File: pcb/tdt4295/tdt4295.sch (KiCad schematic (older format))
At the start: 44 parts, among them J101 ARM 20 Pin Debug Header, J102 DM1AA-SF-PEJ(21), J103 MCU USART1 Header, J104 MCU GPIO Header, U101 EFM32GG12B810F1024GQ64, U102 COM-09032 Joystick, U103 COM-09032 Joystick, Y101 48MHz

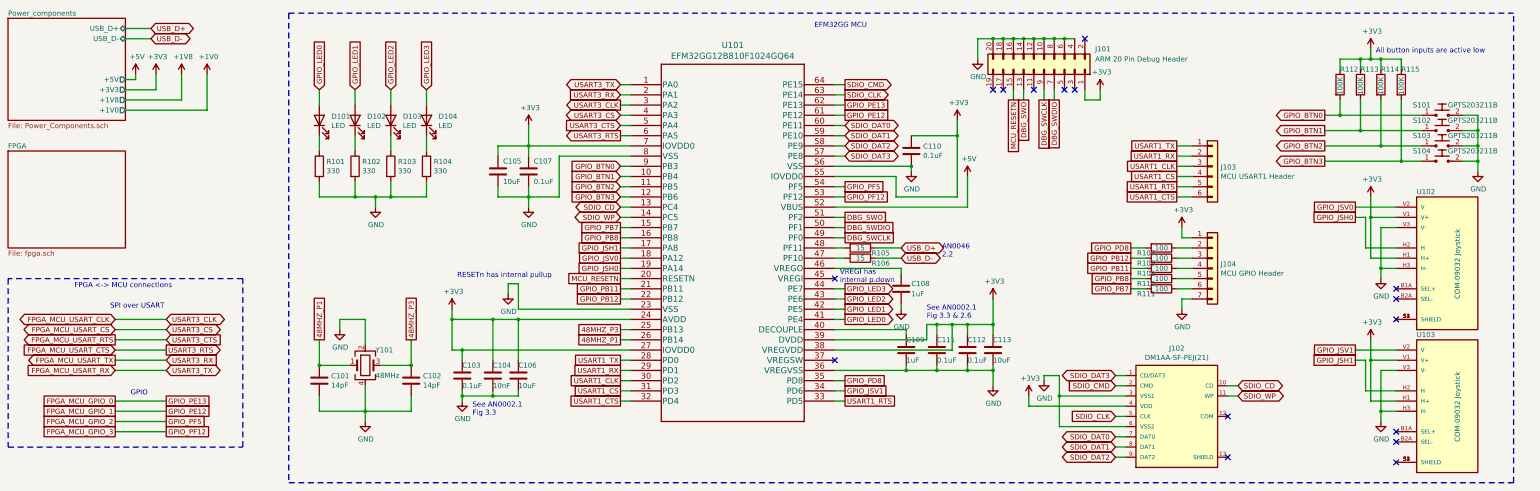
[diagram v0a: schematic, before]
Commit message: MCU fixes from review comments
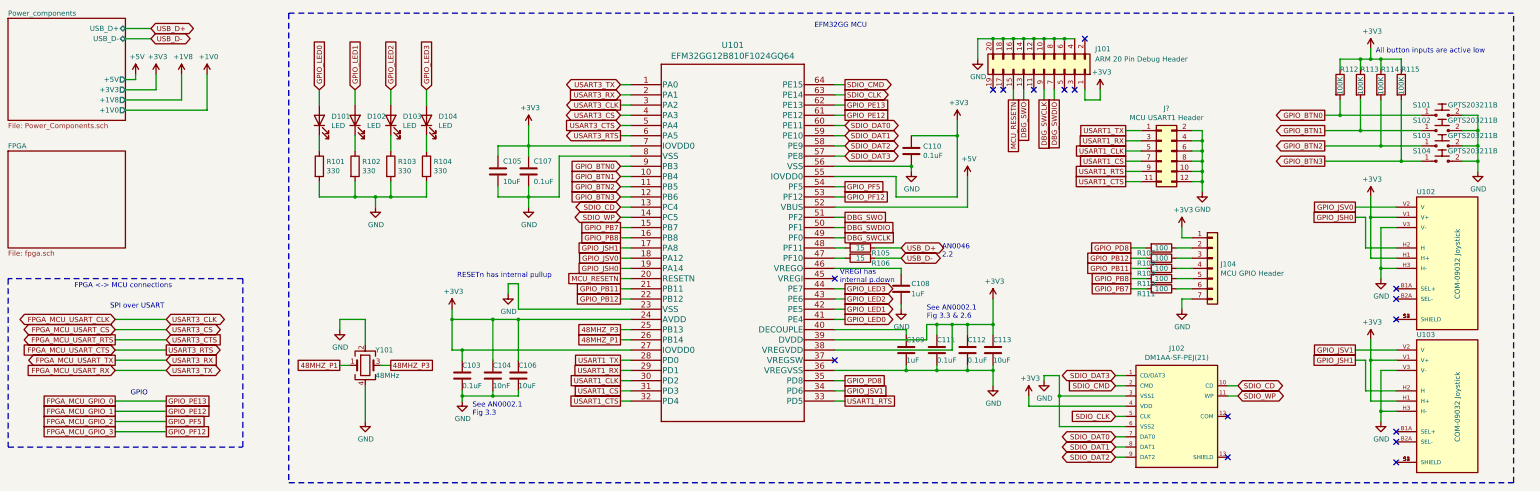
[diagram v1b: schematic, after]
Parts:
- removed C101, C102: 14pF, Capacitor_SMD:C_1210_3225Metric_Pad1.33x2.70mm_HandSolder, symbol Device:C
- removed J103: MCU USART1 Header, Connector_PinSocket_2.54mm:PinSocket_1x06_P2.54mm_Vertical, symbol Connector_Generic:Conn_01x06
- added J?: MCU USART1 Header, symbol Connector_Generic:Conn_02x06_Odd_Even
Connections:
- net GND: now also J?.10 (Pin_10), J?.12 (Pin_12), J?.2 (Pin_2), J?.4 (Pin_4), J?.6 (Pin_6), J?.8 (Pin_8)
- net USART1_CLK: now also J?.5 (Pin_5)
- net USART1_CS: now also J?.7 (Pin_7)
- net USART1_CTS: now also J?.11 (Pin_11)
- net USART1_RTS: now also J?.9 (Pin_9)
- net USART1_RX: now also J?.3 (Pin_3)
- net USART1_TX: now also J?.1 (Pin_1)
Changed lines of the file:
@@
 	4000 3900 4000 4000
 Wire Wire Line
-	4400 4350 4700 4350
-Wire Wire Line
-	4250 4900 4250 4800
-Wire Wire Line
-	4250 4550 4250 4800
-Connection ~ 4250 4800
-Wire Wire Line
-	3800 4800 3800 4650
-Wire Wire Line
-	4250 4800 3800 4800
-Wire Wire Line
-	4700 4800 4700 4650
-Wire Wire Line
-	4250 4800 4700 4800
+	4400 4350 4500 4350
 Wire Wire Line
 	4250 4150 4250 3900
@@
 $EndComp
 $Comp
-L Device:C C102
-U 1 1 6146ECCE
-P 4700 4500
-F 0 "C102" H 4815 4546 50  0000 L CNN
-F 1 "14pF" H 4815 4455 50  0000 L CNN
-F 2 "Capacitor_SMD:C_1210_3225Metric_Pad1.33x2.70mm_HandSolder" H 4738 4350 50  0001 C CNN
-F 3 "https://api.kemet.com/component-edge/download/specsheet/C1210C107M9PACTU.pdf" H 4700 4500 50  0001 C CNN
-F 4 "" H 4700 4500 50  0001 C CNN "Category"
-F 5 "https://no.farnell.com/kemet/c1210c107m9pactu/cap-100-f-6-3v-20-x5r-1210/dp/1108328?st=c1210c107m9pactu" H 4700 4500 50  0001 C CNN "DK_Detail_Page"
-F 6 "C1210C107M9PACTU" H 4700 4500 50  0001 C CNN "Component name"
-	1    4700 4500
-	1    0    0    -1
-$EndComp
-$Comp
-L Device:C C101
-U 1 1 6146E505
-P 3800 4500
-F 0 "C101" H 3915 4546 50  0000 L CNN
-F 1 "14pF" H 3915 4455 50  0000 L CNN
-F 2 "Capacitor_SMD:C_1210_3225Metric_Pad1.33x2.70mm_HandSolder" H 3838 4350 50  0001 C CNN
-F 3 "https://api.kemet.com/component-edge/download/specsheet/C1210C107M9PACTU.pdf" H 3800 4500 50  0001 C CNN
-F 4 "" H 3800 4500 50  0001 C CNN "Category"
-F 5 "https://no.farnell.com/kemet/c1210c107m9pactu/cap-100-f-6-3v-20-x5r-1210/dp/1108328?st=c1210c107m9pactu" H 3800 4500 50  0001 C CNN "DK_Detail_Page"
-F 6 "C1210C107M9PACTU" H 3800 4500 50  0001 C CNN "Component name"
-	1    3800 4500
-	1    0    0    -1
-$EndComp
-$Comp
 L power:GND #PWR0106
 U 1 1 6146D608
@@
 	1    0    0    -1
 $EndComp
-Text GLabel 4700 4100 1    50   UnSpc ~ 0
+Text GLabel 4500 4350 2    50   UnSpc ~ 0
 48MHZ_P3
-Text GLabel 3800 4100 1    50   UnSpc ~ 0
+Text GLabel 4000 4350 0    50   UnSpc ~ 0
 48MHZ_P1
 Wire Wire Line
-	3800 4100 3800 4350
-Wire Wire Line
-	4700 4100 4700 4350
-Connection ~ 4700 4350
-Wire Wire Line
-	3800 4350 4100 4350
-Connection ~ 3800 4350
+	4000 4350 4100 4350
 Text GLabel 6750 4000 0    50   UnSpc ~ 0
 48MHZ_P3
@@
 Text GLabel 11750 3200 0    50   UnSpc ~ 0
 GPIO_PD8
-$Comp
-L Connector_Generic:Conn_01x06 J103
-U 1 1 61BFE8BD
-P 12550 2400
-F 0 "J103" H 12630 2392 50  0000 L CNN
-F 1 "MCU USART1 Header" H 12630 2301 50  0000 L CNN
-F 2 "Connector_PinSocket_2.54mm:PinSocket_1x06_P2.54mm_Vertical" H 12550 2400 50  0001 C CNN
-F 3 "~" H 12550 2400 50  0001 C CNN
-	1    12550 2400
-	1    0    0    -1
-$EndComp
-Text GLabel 12200 2200 0    50   UnSpc ~ 0
+Text GLabel 11700 2050 0    50   UnSpc ~ 0
 USART1_TX
-Text GLabel 12200 2300 0    50   UnSpc ~ 0
+Text GLabel 11700 2150 0    50   UnSpc ~ 0
 USART1_RX
-Text GLabel 12200 2400 0    50   UnSpc ~ 0
+Text GLabel 11700 2250 0    50   UnSpc ~ 0
 USART1_CLK
-Text GLabel 12200 2500 0    50   UnSpc ~ 0
+Text GLabel 11700 2350 0    50   UnSpc ~ 0
 USART1_CS
-Text GLabel 12200 2600 0    50   UnSpc ~ 0
+Text GLabel 11700 2450 0    50   UnSpc ~ 0
 USART1_RTS
-Text GLabel 12200 2700 0    50   UnSpc ~ 0
+Text GLabel 11700 2550 0    50   UnSpc ~ 0
 USART1_CTS
 Wire Wire Line
-	12200 2200 12350 2200
-Wire Wire Line
-	12350 2300 12200 2300
-Wire Wire Line
-	12200 2400 12350 2400
-Wire Wire Line
-	12350 2500 12200 2500
-Wire Wire Line
-	12200 2600 12350 2600
-Wire Wire Line
-	12350 2700 12200 2700
+	11700 2050 11850 2050
+Wire Wire Line
+	11850 2150 11700 2150
+Wire Wire Line
+	11700 2250 11850 2250
+Wire Wire Line
+	11850 2350 11700 2350
+Wire Wire Line
+	11700 2450 11850 2450
+Wire Wire Line
+	11850 2550 11700 2550
 $Comp
 L power:GND #PWR0130
@@
 Text GLabel 11600 4550 0    50   Input ~ 0
 SDIO_CMD
+$Comp
+L Connector_Generic:Conn_02x06_Odd_Even J?
+U 1 1 61568E09
+P 12050 2250
+F 0 "J?" H 12100 2667 50  0000 C CNN
+F 1 "MCU USART1 Header" H 12100 2576 50  0000 C CNN
+F 2 "" H 12050 2250 50  0001 C CNN
+F 3 "~" H 12050 2250 50  0001 C CNN
+	1    12050 2250
+	1    0    0    -1
+$EndComp
+$Comp
+L power:GND #PWR?
+U 1 1 61580AEB
+P 12450 2650
+F 0 "#PWR?" H 12450 2400 50  0001 C CNN
+F 1 "GND" H 12455 2477 50  0000 C CNN
+F 2 "" H 12450 2650 50  0001 C CNN
+F 3 "" H 12450 2650 50  0001 C CNN
+	1    12450 2650
+	1    0    0    -1
+$EndComp
+Wire Wire Line
+	12450 2650 12450 2550
+Wire Wire Line
+	12450 2550 12350 2550
+Wire Wire Line
+	12450 2550 12450 2450
+Wire Wire Line
+	12450 2450 12350 2450
+Connection ~ 12450 2550
+Wire Wire Line
+	12350 2350 12450 2350
+Wire Wire Line
+	12450 2350 12450 2450
+Connection ~ 12450 2450
+Wire Wire Line
+	12350 2250 12450 2250
+Wire Wire Line
+	12450 2250 12450 2350
+Connection ~ 12450 2350
+Wire Wire Line
+	12350 2150 12450 2150
+Wire Wire Line
+	12450 2150 12450 2250
+Connection ~ 12450 2250
+Wire Wire Line
+	12350 2050 12450 2050
+Wire Wire Line
+	12450 2050 12450 2150
+Connection ~ 12450 2150
+Wire Wire Line
+	4250 4550 4250 4900
 $EndSCHEMATC

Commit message: add footprints, rename components
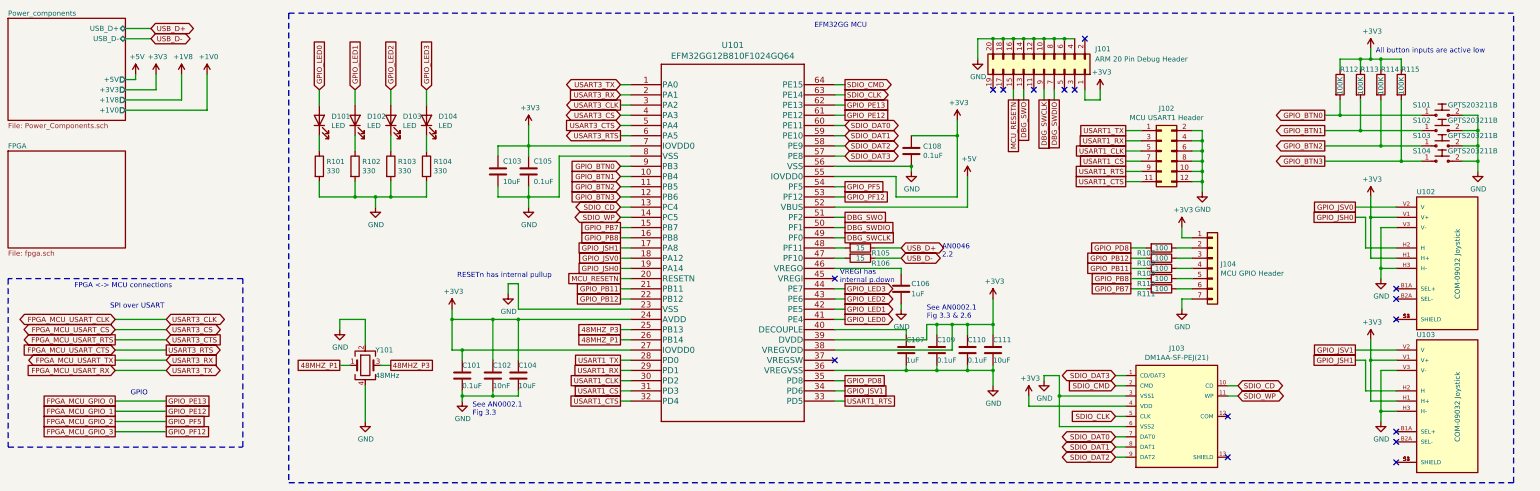
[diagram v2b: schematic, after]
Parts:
- J102: renamed from J?; footprint (none) -> Connector_PinHeader_2.54mm:PinHeader_2x06_P2.54mm_Vertical
- renumbered C103 to C101, C104 to C102, C105 to C103, C106 to C104, C107 to C105, C108 to C106, C109 to C107, C110 to C108, C111 to C109, C112 to C110, C113 to C111, J102 to J103
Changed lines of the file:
@@
 	10050 1950 10050 2100
 $Comp
-L Device:C C110
+L Device:C C108
 U 1 1 614780F2
 P 9600 2250
-F 0 "C110" H 9715 2296 50  0000 L CNN
+F 0 "C108" H 9715 2296 50  0000 L CNN
 F 1 "0.1uF" H 9715 2205 50  0000 L CNN
 F 2 "Capacitor_SMD:C_0603_1608Metric_Pad1.08x0.95mm_HandSolder" H 9638 2100 50  0001 C CNN
@@
 $EndComp
 $Comp
-L Device:C C103
+L Device:C C101
 U 1 1 614CD408
 P 5200 4450
-F 0 "C103" H 5200 4550 50  0000 L CNN
+F 0 "C101" H 5200 4550 50  0000 L CNN
 F 1 "0.1uF" H 5200 4350 50  0000 L CNN
 F 2 "Capacitor_SMD:C_0603_1608Metric_Pad1.08x0.95mm_HandSolder" H 5238 4300 50  0001 C CNN
@@
 Connection ~ 5200 4200
 $Comp
-L Device:C C107
+L Device:C C105
 U 1 1 614EE588
 P 5850 2450
-F 0 "C107" H 5900 2550 50  0000 L CNN
+F 0 "C105" H 5900 2550 50  0000 L CNN
 F 1 "0.1uF" H 5900 2350 50  0000 L CNN
 F 2 "Capacitor_SMD:C_0603_1608Metric_Pad1.08x0.95mm_HandSolder" H 5888 2300 50  0001 C CNN
@@
 Connection ~ 5850 2200
 $Comp
-L Device:C C105
+L Device:C C103
 U 1 1 6153B508
 P 5550 2450
-F 0 "C105" H 5600 2550 50  0000 L CNN
+F 0 "C103" H 5600 2550 50  0000 L CNN
 F 1 "10uF" H 5600 2350 50  0000 L CNN
 F 2 "Capacitor_SMD:C_0603_1608Metric_Pad1.08x0.95mm_HandSolder" H 5588 2300 50  0001 C CNN
@@
 	5850 2200 6850 2200
 $Comp
-L Device:C C109
+L Device:C C107
 U 1 1 6145F357
 P 9550 4200
-F 0 "C109" H 9550 4300 50  0000 L CNN
+F 0 "C107" H 9550 4300 50  0000 L CNN
 F 1 "1uF" H 9550 4100 50  0000 L CNN
 F 2 "Capacitor_SMD:C_0603_1608Metric_Pad1.08x0.95mm_HandSolder" H 9588 4050 50  0001 C CNN
@@
 $EndComp
 $Comp
-L Device:C C104
+L Device:C C102
 U 1 1 615F1A43
 P 5500 4450
-F 0 "C104" H 5500 4550 50  0000 L CNN
+F 0 "C102" H 5500 4550 50  0000 L CNN
 F 1 "10nF" H 5500 4350 50  0000 L CNN
 F 2 "Capacitor_SMD:C_0603_1608Metric_Pad1.08x0.95mm_HandSolder" H 5538 4300 50  0001 C CNN
@@
 $EndComp
 $Comp
-L Device:C C106
+L Device:C C104
 U 1 1 615F24C1
 P 5750 4450
-F 0 "C106" H 5750 4550 50  0000 L CNN
+F 0 "C104" H 5750 4550 50  0000 L CNN
 F 1 "10uF" H 5750 4350 50  0000 L CNN
 F 2 "Capacitor_SMD:C_0603_1608Metric_Pad1.08x0.95mm_HandSolder" H 5788 4300 50  0001 C CNN
@@
 $EndComp
 $Comp
-L Device:C C113
+L Device:C C111
 U 1 1 61654772
 P 10400 4200
-F 0 "C113" H 10400 4300 50  0000 L CNN
+F 0 "C111" H 10400 4300 50  0000 L CNN
 F 1 "10uF" H 10400 4100 50  0000 L CNN
 F 2 "Capacitor_SMD:C_0603_1608Metric_Pad1.08x0.95mm_HandSolder" H 10438 4050 50  0001 C CNN
@@
 $EndComp
 $Comp
-L Device:C C112
+L Device:C C110
 U 1 1 61654C00
 P 10150 4200
-F 0 "C112" H 10150 4300 50  0000 L CNN
+F 0 "C110" H 10150 4300 50  0000 L CNN
 F 1 "0.1uF" H 10150 4100 50  0000 L CNN
 F 2 "Capacitor_SMD:C_0603_1608Metric_Pad1.08x0.95mm_HandSolder" H 10188 4050 50  0001 C CNN
@@
 	10000 3950 10150 3950
 $Comp
-L Device:C C111
+L Device:C C109
 U 1 1 61724FBA
 P 9850 4200
-F 0 "C111" H 9850 4300 50  0000 L CNN
+F 0 "C109" H 9850 4300 50  0000 L CNN
 F 1 "0.1uF" H 9850 4100 50  0000 L CNN
 F 2 "Capacitor_SMD:C_0603_1608Metric_Pad1.08x0.95mm_HandSolder" H 9888 4050 50  0001 C CNN
@@
 AN0046\n2.2
 $Comp
-L Device:C C108
+L Device:C C106
 U 1 1 618F8B31
 P 9500 3600
-F 0 "C108" H 9600 3650 50  0000 L CNN
+F 0 "C106" H 9600 3650 50  0000 L CNN
 F 1 "1uF" H 9600 3550 50  0000 L CNN
 F 2 "Capacitor_SMD:C_0603_1608Metric_Pad1.08x0.95mm_HandSolder" H 9538 3450 50  0001 C CNN
@@
 	15150 1900 15000 1900
 $Comp
-L power:+3V3 #PWR0125
+L power:+3V3 #PWR0126
 U 1 1 614E0EAB
 P 14100 1250
-F 0 "#PWR0125" H 14100 1100 50  0001 C CNN
+F 0 "#PWR0126" H 14100 1100 50  0001 C CNN
 F 1 "+3V3" H 14115 1423 50  0000 C CNN
 F 2 "" H 14100 1250 50  0001 C CNN
@@
 	11850 2550 11700 2550
 $Comp
-L power:GND #PWR0130
+L power:GND #PWR0131
 U 1 1 615042CB
 P 15150 2450
-F 0 "#PWR0130" H 15150 2200 50  0001 C CNN
+F 0 "#PWR0131" H 15150 2200 50  0001 C CNN
 F 1 "GND" H 15155 2277 50  0000 C CNN
 F 2 "" H 15150 2450 50  0001 C CNN
@@
 NoConn ~ 14350 3900
 $Comp
-L power:+3V3 #PWR0126
+L power:+3V3 #PWR0127
 U 1 1 615D21D5
 P 14100 2700
-F 0 "#PWR0126" H 14100 2550 50  0001 C CNN
+F 0 "#PWR0127" H 14100 2550 50  0001 C CNN
 F 1 "+3V3" H 14115 2873 50  0000 C CNN
 F 2 "" H 14100 2700 50  0001 C CNN
@@
 NoConn ~ 14350 3700
 $Comp
-L power:GND #PWR0128
+L power:GND #PWR0129
 U 1 1 61621364
 P 14200 3500
-F 0 "#PWR0128" H 14200 3250 50  0001 C CNN
+F 0 "#PWR0129" H 14200 3250 50  0001 C CNN
 F 1 "GND" H 14205 3327 50  0000 C CNN
 F 2 "" H 14200 3500 50  0001 C CNN
@@
 NoConn ~ 14350 5300
 $Comp
-L power:+3V3 #PWR0127
+L power:+3V3 #PWR0128
 U 1 1 616BCC96
 P 14100 4100
-F 0 "#PWR0127" H 14100 3950 50  0001 C CNN
+F 0 "#PWR0128" H 14100 3950 50  0001 C CNN
 F 1 "+3V3" H 14115 4273 50  0000 C CNN
 F 2 "" H 14100 4100 50  0001 C CNN
@@
 NoConn ~ 14350 5100
 $Comp
-L power:GND #PWR0129
+L power:GND #PWR0130
 U 1 1 616BCCA3
 P 14200 4900
-F 0 "#PWR0129" H 14200 4650 50  0001 C CNN
+F 0 "#PWR0130" H 14200 4650 50  0001 C CNN
 F 1 "GND" H 14205 4727 50  0000 C CNN
 F 2 "" H 14200 4900 50  0001 C CNN
@@
 NoConn ~ 12700 4850
 $Comp
-L DM1AA-SF-PEJ_21_:DM1AA-SF-PEJ(21) J102
+L DM1AA-SF-PEJ_21_:DM1AA-SF-PEJ(21) J103
 U 1 1 61599B42
 P 12200 4850
-F 0 "J102" H 12200 5517 50  0000 C CNN
+F 0 "J103" H 12200 5517 50  0000 C CNN
 F 1 "DM1AA-SF-PEJ(21)" H 12200 5426 50  0000 C CNN
 F 2 "HRS_DM1AA-SF-PEJ(21)" H 12200 4850 50  0001 L BNN
@@
 SDIO_CMD
 $Comp
-L Connector_Generic:Conn_02x06_Odd_Even J?
+L Connector_Generic:Conn_02x06_Odd_Even J102
 U 1 1 61568E09
 P 12050 2250
-F 0 "J?" H 12100 2667 50  0000 C CNN
+F 0 "J102" H 12100 2667 50  0000 C CNN
 F 1 "MCU USART1 Header" H 12100 2576 50  0000 C CNN
-F 2 "" H 12050 2250 50  0001 C CNN
+F 2 "Connector_PinHeader_2.54mm:PinHeader_2x06_P2.54mm_Vertical" H 12050 2250 50  0001 C CNN
 F 3 "~" H 12050 2250 50  0001 C CNN
 	1    12050 2250
@@
 $EndComp
 $Comp
-L power:GND #PWR?
+L power:GND #PWR0125
 U 1 1 61580AEB
 P 12450 2650
-F 0 "#PWR?" H 12450 2400 50  0001 C CNN
+F 0 "#PWR0125" H 12450 2400 50  0001 C CNN
 F 1 "GND" H 12455 2477 50  0000 C CNN
 F 2 "" H 12450 2650 50  0001 C CNN

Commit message: footprints for everything
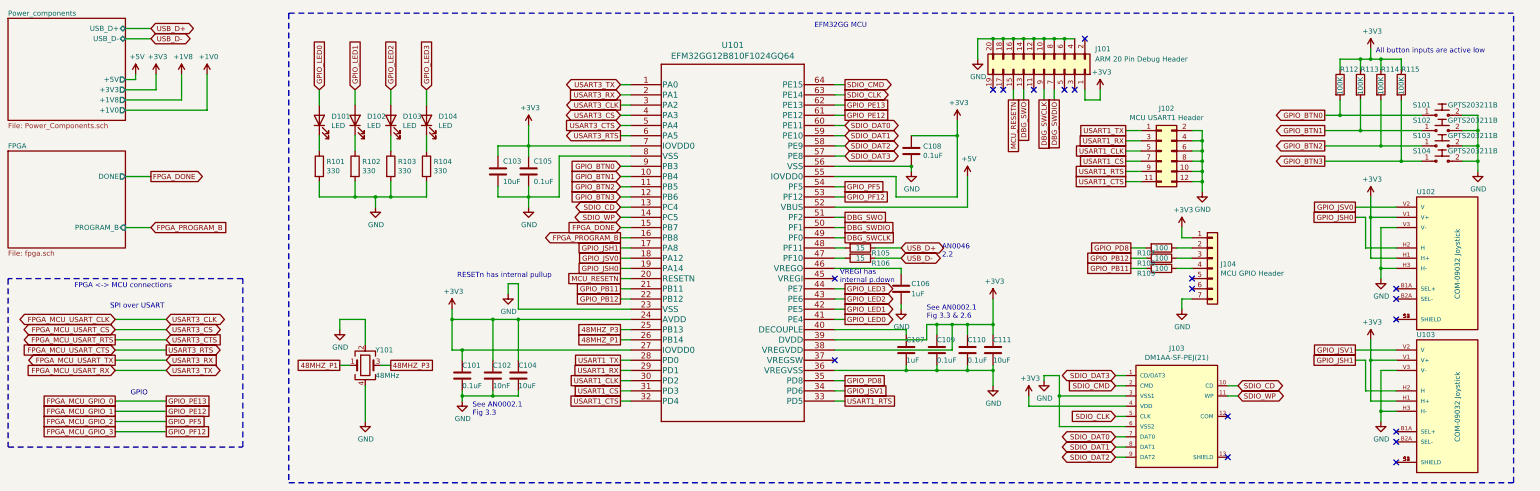
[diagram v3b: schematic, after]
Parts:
- removed R110, R111: 100, Resistor_SMD:R_0805_2012Metric_Pad1.20x1.40mm_HandSolder, symbol Device:R
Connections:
- net GPIO_PB7 renamed FPGA_DONE
- net GPIO_PB8 renamed FPGA_PROGRAM_B
- no-connect marks 16 -> 18
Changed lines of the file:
@@
 Text GLabel 8950 3600 2    50   Output ~ 0
 GPIO_LED3
-Text GLabel 6750 3000 0    50   UnSpc ~ 0
-GPIO_PB7
+Text GLabel 6750 3000 0    50   Input ~ 0
+FPGA_DONE
 Text GLabel 8950 1800 2    50   UnSpc ~ 0
 GPIO_PE13
@@
 F0 "FPGA" 50
 F1 "fpga.sch" 50
+F2 "DONE" O R 1900 2500 50
+F3 "PROGRAM_B" I R 1900 3000 50
 $EndSheet
 Text GLabel 1800 3900 0    50   BiDi ~ 0
@@
 Wire Wire Line
 	12250 3700 12250 3800
-Text GLabel 11750 3600 0    50   UnSpc ~ 0
-GPIO_PB7
 Text GLabel 2300 4700 2    50   UnSpc ~ 0
 GPIO_PE13
@@
 Text Notes 1400 3600 0    50   ~ 0
 FPGA <-> MCU connections
-Text GLabel 6750 3100 0    50   UnSpc ~ 0
-GPIO_PB8
+Text GLabel 6750 3100 0    50   Output ~ 0
+FPGA_PROGRAM_B
 Text GLabel 6750 3600 0    50   UnSpc ~ 0
 GPIO_PB11
 Text GLabel 6750 3700 0    50   UnSpc ~ 0
 GPIO_PB12
-Text GLabel 11750 3500 0    50   UnSpc ~ 0
-GPIO_PB8
 Text GLabel 11750 3400 0    50   UnSpc ~ 0
 GPIO_PB11
@@
 	0    1    1    0
 $EndComp
-$Comp
-L Device:R R110
-U 1 1 6153AB74
-P 12050 3500
-F 0 "R110" V 12100 3350 50  0000 C CNN
-F 1 "100" V 12050 3500 50  0000 C CNN
-F 2 "Resistor_SMD:R_0805_2012Metric_Pad1.20x1.40mm_HandSolder" V 11980 3500 50  0001 C CNN
-F 3 "https://www.vishay.com/docs/28705/mcx0x0xpro.pdf" H 12050 3500 50  0001 C CNN
-F 4 "MCU08050C1000FP500" H 12050 3500 50  0001 C CNN "Category"
-F 5 "https://www.digikey.no/product-detail/no/vishay-beyschlag-draloric-bc-components/MCU08050C1000FP500/MCU0805-100-CFCT-ND/2607922" H 12050 3500 50  0001 C CNN "DK_Detail_Page"
-	1    12050 3500
-	0    1    1    0
-$EndComp
-$Comp
-L Device:R R111
-U 1 1 6153ACD0
-P 12050 3600
-F 0 "R111" V 12100 3450 50  0000 C CNN
-F 1 "100" V 12050 3600 50  0000 C CNN
-F 2 "Resistor_SMD:R_0805_2012Metric_Pad1.20x1.40mm_HandSolder" V 11980 3600 50  0001 C CNN
-F 3 "https://www.vishay.com/docs/28705/mcx0x0xpro.pdf" H 12050 3600 50  0001 C CNN
-F 4 "MCU08050C1000FP500" H 12050 3600 50  0001 C CNN "Category"
-F 5 "https://www.digikey.no/product-detail/no/vishay-beyschlag-draloric-bc-components/MCU08050C1000FP500/MCU0805-100-CFCT-ND/2607922" H 12050 3600 50  0001 C CNN "DK_Detail_Page"
-	1    12050 3600
-	0    1    1    0
-$EndComp
 Wire Wire Line
 	11900 3200 11750 3200
@@
 Wire Wire Line
 	11900 3400 11750 3400
-Wire Wire Line
-	11750 3500 11900 3500
-Wire Wire Line
-	11900 3600 11750 3600
-Wire Wire Line
-	12200 3600 12350 3600
-Wire Wire Line
-	12350 3500 12200 3500
 Wire Wire Line
 	12200 3400 12350 3400
@@
 Wire Wire Line
 	4250 4550 4250 4900
+NoConn ~ 12350 3500
+NoConn ~ 12350 3600
+Text GLabel 2150 2500 2    50   Output ~ 0
+FPGA_DONE
+Text GLabel 2150 3000 2    50   Input ~ 0
+FPGA_PROGRAM_B
+Wire Wire Line
+	2150 2500 1900 2500
+Wire Wire Line
+	1900 3000 2150 3000
 $EndSCHEMATC
